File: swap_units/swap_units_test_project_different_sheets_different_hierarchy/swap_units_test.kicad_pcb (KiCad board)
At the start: 2 copper layers, 22 parts, among them U1 LM324, U2 PIC18F452-IP, U3 LM324, U7 LM324, U8 LM324

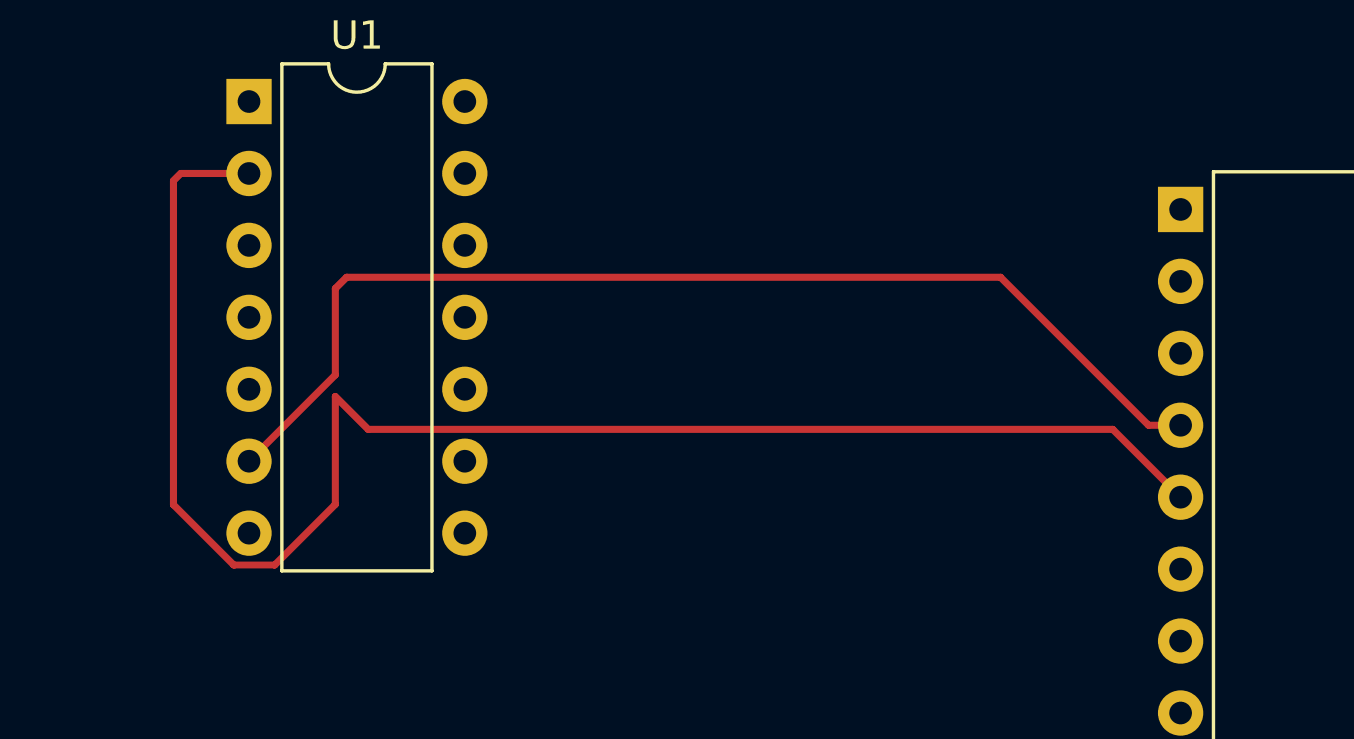
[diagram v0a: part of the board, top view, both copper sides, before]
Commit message: updated reference test projects
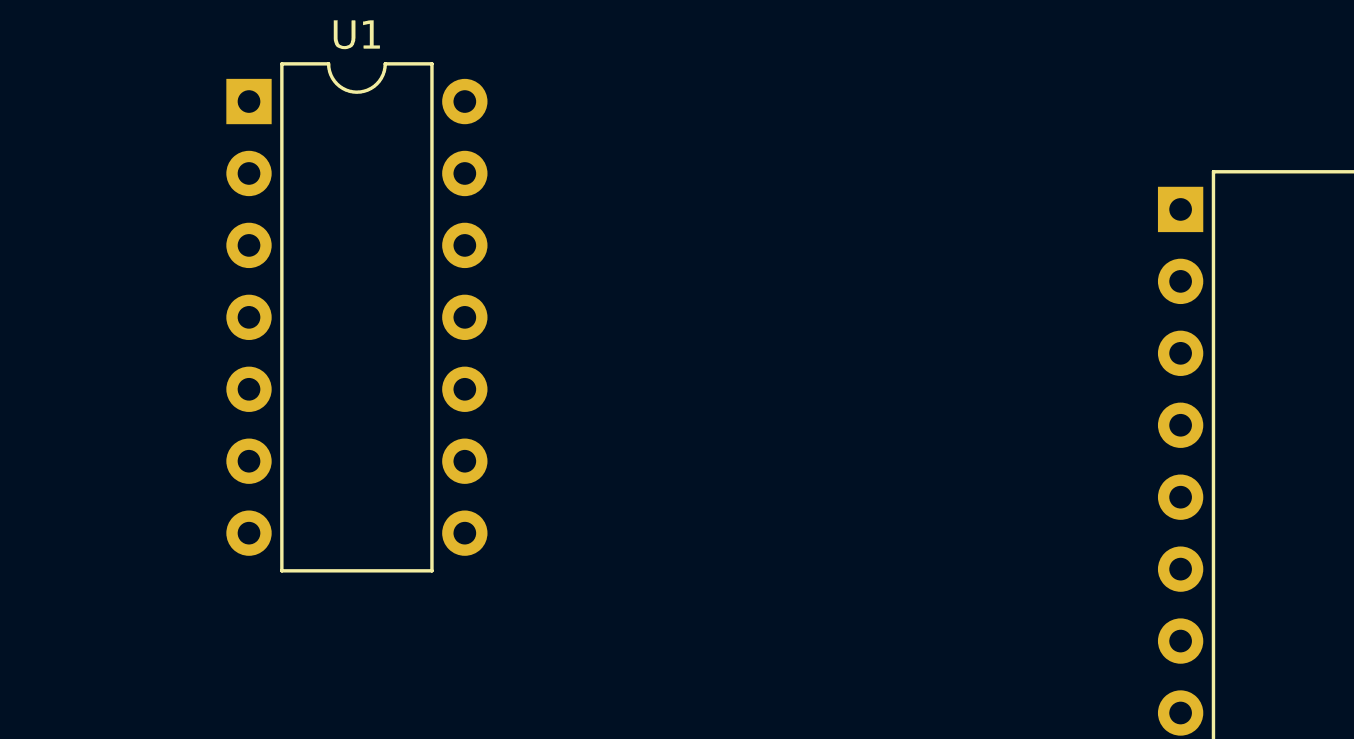
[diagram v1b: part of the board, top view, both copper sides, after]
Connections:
- U1 pad 1: Net-(U1-Pad6) -> Net-(U1-Pad1)
- U1 pad 10: Net-(R6-Pad2) -> Net-(R4-Pad2)
- U1 pad 12: Net-(R4-Pad2) -> Net-(R6-Pad2)
- U1 pad 13: /Level1/out_level_1 -> /Level1/out_level_2
- U1 pad 14: /Level1/out_level_1 -> /Level1/out_level_2
- U1 pad 2: Net-(U1-Pad6) -> Net-(U1-Pad1)
- U1 pad 3: Net-(R2-Pad2) -> Net-(R1-Pad2)
- U1 pad 5: Net-(R1-Pad2) -> Net-(R2-Pad2)
- U1 pad 6: Net-(U1-Pad1) -> Net-(U1-Pad6)
- U1 pad 7: Net-(U1-Pad1) -> Net-(U1-Pad6)
- U1 pad 8: /Level1/out_level_2 -> /Level1/out_level_1
- U1 pad 9: /Level1/out_level_2 -> /Level1/out_level_1
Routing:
- net Net-(U1-Pad6): track 56.8 -> 0.00 mm
- net Net-(U1-Pad1): track 39.5 -> 0.00 mm
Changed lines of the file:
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@@
     (thickness 1.6)
     (drawings 0)
-    (tracks 16)
+    (tracks 0)
     (zones 0)
     (modules 22)
@@
     )
     (pad 1 thru_hole rect (at 0 0) (size 1.6 1.6) (drill 0.8) (layers *.Cu *.Mask)
-      (net 9 "Net-(U1-Pad6)"))
+      (net 7 "Net-(U1-Pad1)"))
     (pad 8 thru_hole oval (at 7.62 15.24) (size 1.6 1.6) (drill 0.8) (layers *.Cu *.Mask)
-      (net 10 /Level1/out_level_2))
+      (net 8 /Level1/out_level_1))
     (pad 2 thru_hole oval (at 0 2.54) (size 1.6 1.6) (drill 0.8) (layers *.Cu *.Mask)
-      (net 9 "Net-(U1-Pad6)"))
+      (net 7 "Net-(U1-Pad1)"))
     (pad 9 thru_hole oval (at 7.62 12.7) (size 1.6 1.6) (drill 0.8) (layers *.Cu *.Mask)
-      (net 10 /Level1/out_level_2))
+      (net 8 /Level1/out_level_1))
     (pad 3 thru_hole oval (at 0 5.08) (size 1.6 1.6) (drill 0.8) (layers *.Cu *.Mask)
-      (net 3 "Net-(R2-Pad2)"))
+      (net 2 "Net-(R1-Pad2)"))
     (pad 10 thru_hole oval (at 7.62 10.16) (size 1.6 1.6) (drill 0.8) (layers *.Cu *.Mask)
-      (net 6 "Net-(R6-Pad2)"))
+      (net 5 "Net-(R4-Pad2)"))
     (pad 4 thru_hole oval (at 0 7.62) (size 1.6 1.6) (drill 0.8) (layers *.Cu *.Mask)
       (net 1 +5V))
@@
       (net 4 GND))
     (pad 5 thru_hole oval (at 0 10.16) (size 1.6 1.6) (drill 0.8) (layers *.Cu *.Mask)
-      (net 2 "Net-(R1-Pad2)"))
+      (net 3 "Net-(R2-Pad2)"))
     (pad 12 thru_hole oval (at 7.62 5.08) (size 1.6 1.6) (drill 0.8) (layers *.Cu *.Mask)
-      (net 5 "Net-(R4-Pad2)"))
+      (net 6 "Net-(R6-Pad2)"))
     (pad 6 thru_hole oval (at 0 12.7) (size 1.6 1.6) (drill 0.8) (layers *.Cu *.Mask)
-      (net 7 "Net-(U1-Pad1)"))
+      (net 9 "Net-(U1-Pad6)"))
     (pad 13 thru_hole oval (at 7.62 2.54) (size 1.6 1.6) (drill 0.8) (layers *.Cu *.Mask)
-      (net 8 /Level1/out_level_1))
+      (net 10 /Level1/out_level_2))
     (pad 7 thru_hole oval (at 0 15.24) (size 1.6 1.6) (drill 0.8) (layers *.Cu *.Mask)
-      (net 7 "Net-(U1-Pad1)"))
+      (net 9 "Net-(U1-Pad6)"))
     (pad 14 thru_hole oval (at 7.62 0) (size 1.6 1.6) (drill 0.8) (layers *.Cu *.Mask)
-      (net 8 /Level1/out_level_1))
+      (net 10 /Level1/out_level_2))
     (model ${KISYS3DMOD}/Package_DIP.3dshapes/DIP-14_W7.62mm.wrl
       (at (xyz 0 0 0))
@@
     )
   )
-  (segment (start 132.708631 58.021001) (end 109.618999 58.021001) (width 0.25) (layer F.Cu) (net 7))
-  (segment (start 139.065 63.246) (end 137.93363 63.246) (width 0.25) (layer F.Cu) (net 7))
-  (segment (start 137.93363 63.246) (end 132.708631 58.021001) (width 0.25) (layer F.Cu) (net 7))
-  (segment (start 109.618999 58.021001) (end 109.22 58.42) (width 0.25) (layer F.Cu) (net 7))
-  (segment (start 109.22 61.468) (end 106.172 64.516) (width 0.25) (layer F.Cu) (net 7))
-  (segment (start 109.22 58.42) (end 109.22 61.468) (width 0.25) (layer F.Cu) (net 7))
-  (segment (start 136.669999 63.390999) (end 110.380999 63.390999) (width 0.25) (layer F.Cu) (net 9))
-  (segment (start 139.065 65.786) (end 136.669999 63.390999) (width 0.25) (layer F.Cu) (net 9))
-  (segment (start 110.380999 63.390999) (end 109.22 62.23) (width 0.25) (layer F.Cu) (net 9))
-  (segment (start 109.22 62.23) (end 109.22 66.04) (width 0.25) (layer F.Cu) (net 9))
-  (segment (start 105.631999 68.181001) (end 103.505 66.054002) (width 0.25) (layer F.Cu) (net 9))
-  (segment (start 109.22 66.04) (end 107.078999 68.181001) (width 0.25) (layer F.Cu) (net 9))
-  (segment (start 107.078999 68.181001) (end 105.631999 68.181001) (width 0.25) (layer F.Cu) (net 9))
-  (segment (start 103.505 66.054002) (end 103.505 54.61) (width 0.25) (layer F.Cu) (net 9))
-  (segment (start 103.759 54.356) (end 106.172 54.356) (width 0.25) (layer F.Cu) (net 9))
-  (segment (start 103.505 54.61) (end 103.759 54.356) (width 0.25) (layer F.Cu) (net 9))
 )

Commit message: updated test projects
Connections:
- U7 pad 13: /Level1/Level3a/out_level_2 -> /Level1/Level3a/out_level_1
- U7 pad 14: /Level1/Level3a/out_level_2 -> /Level1/Level3a/out_level_1
- U8 pad 13: /Level1/Level3b/out_level_2 -> /Level1/Level3b/out_level_1
- U8 pad 14: /Level1/Level3b/out_level_2 -> /Level1/Level3b/out_level_1
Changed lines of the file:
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@@
     (zones 0)
     (modules 22)
-    (nets 54)
+    (nets 56)
   )
   (page A4)
@@
   (net 52 /Level1/Level3a/out_level_2)
   (net 53 /Level1/Level3b/out_level_2)
+  (net 54 /Level1/Level3a/out_level_1)
+  (net 55 /Level1/Level3b/out_level_1)
   (net_class Default "This is the default net class."
     (clearance 0.2)
@@
     (add_net +5V)
     (add_net /Level1/Level2b/out_level_2)
+    (add_net /Level1/Level3a/out_level_1)
     (add_net /Level1/Level3a/out_level_2)
+    (add_net /Level1/Level3b/out_level_1)
     (add_net /Level1/Level3b/out_level_2)
     (add_net /Level1/out_level_1)
@@
     (fp_arc (start 3.81 -1.33) (end 2.81 -1.33) (angle -180) (layer F.SilkS) (width 0.12))
     (pad 14 thru_hole oval (at 7.62 0) (size 1.6 1.6) (drill 0.8) (layers *.Cu *.Mask)
-      (net 53 /Level1/Level3b/out_level_2))
+      (net 55 /Level1/Level3b/out_level_1))
     (pad 7 thru_hole oval (at 0 15.24) (size 1.6 1.6) (drill 0.8) (layers *.Cu *.Mask)
       (net 53 /Level1/Level3b/out_level_2))
     (pad 13 thru_hole oval (at 7.62 2.54) (size 1.6 1.6) (drill 0.8) (layers *.Cu *.Mask)
-      (net 53 /Level1/Level3b/out_level_2))
+      (net 55 /Level1/Level3b/out_level_1))
     (pad 6 thru_hole oval (at 0 12.7) (size 1.6 1.6) (drill 0.8) (layers *.Cu *.Mask)
       (net 53 /Level1/Level3b/out_level_2))
@@
     (fp_arc (start 3.81 -1.33) (end 2.81 -1.33) (angle -180) (layer F.SilkS) (width 0.12))
     (pad 14 thru_hole oval (at 7.62 0) (size 1.6 1.6) (drill 0.8) (layers *.Cu *.Mask)
-      (net 52 /Level1/Level3a/out_level_2))
+      (net 54 /Level1/Level3a/out_level_1))
     (pad 7 thru_hole oval (at 0 15.24) (size 1.6 1.6) (drill 0.8) (layers *.Cu *.Mask)
       (net 52 /Level1/Level3a/out_level_2))
     (pad 13 thru_hole oval (at 7.62 2.54) (size 1.6 1.6) (drill 0.8) (layers *.Cu *.Mask)
-      (net 52 /Level1/Level3a/out_level_2))
+      (net 54 /Level1/Level3a/out_level_1))
     (pad 6 thru_hole oval (at 0 12.7) (size 1.6 1.6) (drill 0.8) (layers *.Cu *.Mask)
       (net 52 /Level1/Level3a/out_level_2))
